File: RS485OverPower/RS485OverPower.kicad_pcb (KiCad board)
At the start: 2 copper layers, 50 x 45 mm, 27 parts, among them J101 OSTTC022162, J102 OSTTC022162, U101 RT6200, U102 LT1785xS8

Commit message: First layout done
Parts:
- removed R101: R_Small, Resistor_SMD:R_0603_1608Metric
- added C111: 1u/10V, Capacitor_SMD:C_0603_1608Metric, F.Cu at (106.6, 55.0)
- added C112: 1u/10V, Capacitor_SMD:C_0603_1608Metric, F.Cu at (87.7, 78.4)
- C101: footprint Capacitor_SMD:C_0603_1608Metric -> Capacitor_SMD:C_0805_2012Metric
- L101, L102, L103: value 47u -> 33UH; footprint digikey-footprints:1210 -> PCBDecals:MWSA0603
- moved C109 69.3 mm to (74.9, 88.0)
- moved C107 65.9 mm to (75.1, 90.1)
- moved R106 49.6 mm to (83.9, 80.1), turned to 180 degrees
- moved C101 44.3 mm to (101.8, 83.3), turned to 180 degrees
- moved R108 37.4 mm to (100.4, 75.4), turned to 180 degrees
- moved R107 37.1 mm to (104.7, 75.4), turned to 180 degrees
- moved C108 35.8 mm to (109.5, 74.3), turned to 90 degrees
- moved C110 28.9 mm to (111.3, 74.4), turned to 90 degrees
- moved L101 12.5 mm to (110.3, 79.9), turned to 0 degrees
- moved C106 12.0 mm to (107.3, 74.3), turned to 90 degrees
- moved R102 10.8 mm to (101.7, 81.0)
- moved L103 10.5 mm to (90.9, 83.6)
- moved R103 9.71 mm to (99.7, 78.5)
- moved C102 9.71 mm to (98.1, 78.5)
- moved U101 9.71 mm to (102.5, 78.2)
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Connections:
- net Net-(R107-Pad2) renamed /FB
- A101 pad 18: VCC -> Net-(A101-Pad18)
- A101 pad 3: Net-(A101-Pad28) -> Net-(A101-Pad3)
- C103 pad 2: Net-(C103-Pad2) -> /SW
- D101 pad 1: Net-(C103-Pad2) -> /SW
- L101 pad 1: VCC -> /SW
- L101 pad 2: Net-(C103-Pad2) -> VCC
- U101 pad 6: Net-(C103-Pad2) -> /SW
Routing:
- net VCC: track 0.00 -> 56.2 mm
- net +24V: track 23.9 -> 52.9 mm, vias 1 -> 2
- net Net-(A101-Pad1): track 4.16 -> 10.5 mm
- net /FB: track 0.00 -> 6.19 mm
- net Net-(A101-Pad2): track 4.02 -> 9.72 mm
- net Net-(A101-Pad6): track 20.9 -> 15.5 mm
- net Net-(C102-Pad1): track 0.00 -> 5.26 mm
- net GND: track 0.00 -> 4.38 mm, vias 0 -> 19
- net Net-(A101-Pad5): track 15.1 -> 12.6 mm
- net Net-(A101-Pad18): track 0.00 -> 2.34 mm
- net Net-(C103-Pad1): track 0.00 -> 1.88 mm
- net Net-(C104-Pad2): track 2.93 -> 4.57 mm
- net Net-(C105-Pad1): track 3.15 -> 4.57 mm
- net Net-(C105-Pad2): track 10.0 -> 11.1 mm
- net Net-(C104-Pad1): track 10.4 -> 11.0 mm
- added copper zone on B.Cu, net +24V
- added copper zone on F.Cu, net /SW
- added copper zone on B.Cu, net GND
- added copper zone on F.Cu, net GND
- added copper zone on F.Cu, net VCC
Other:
- rule pad_to_mask_clearance: 0 -> 0.1

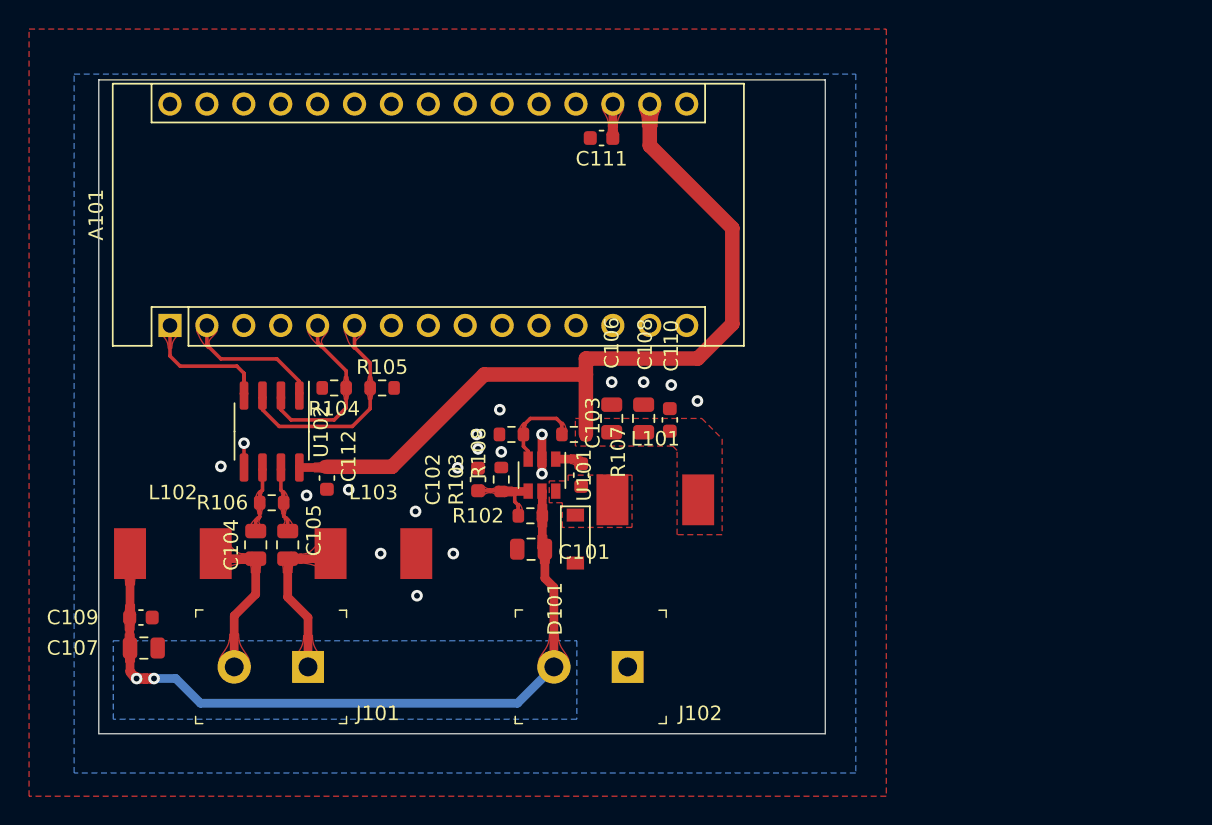
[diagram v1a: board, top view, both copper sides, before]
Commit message: Added connector for I/O
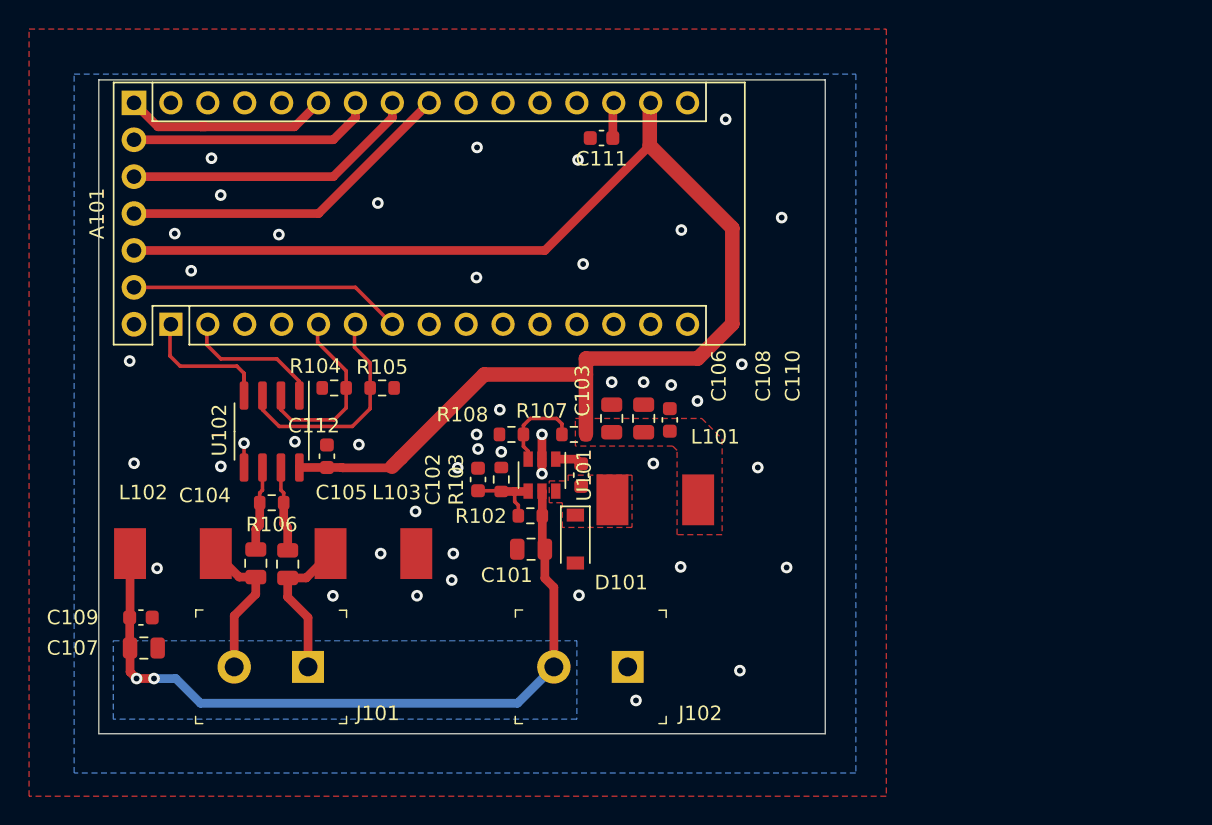
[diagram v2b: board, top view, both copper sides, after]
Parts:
- added J103: Conn_01x07, Connector_PinHeader_2.54mm:PinHeader_1x07_P2.54mm_Vertical, B.Cu at (74.4, 52.6)
- moved C112 1.50 mm to (87.7, 76.9), turned to 90 degrees
- moved C105 1.33 mm to (85.0, 84.3)
- moved C104 1.27 mm to (82.8, 84.3)
- moved A101 0.10 mm to (77.0, 67.8)
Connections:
- A101 pad 23: Net-(A101-Pad23) -> A4
- A101 pad 24: Net-(A101-Pad24) -> A5
- A101 pad 25: Net-(A101-Pad25) -> A6
- A101 pad 26: Net-(A101-Pad26) -> A7
- A101 pad 7: Net-(A101-Pad7) -> D4
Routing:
- net VCC: track 56.2 -> 95.5 mm
- net A4: track 0.00 -> 23.5 mm
- net A7: track 0.00 -> 20.5 mm
- net A5: track 0.00 -> 20.5 mm
- net D4: track 0.00 -> 18.8 mm
- net A6: track 0.00 -> 16.9 mm
- net Net-(C105-Pad1): track 4.57 -> 5.90 mm
- net Net-(C104-Pad2): track 4.57 -> 5.83 mm
- net GND: vias 19 -> 45

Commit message: Layout improvements
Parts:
- added H101: MountingHole, MountingHole:MountingHole_3.2mm_M3, B.Cu at (95.1, 58.5)
- added H102: MountingHole, MountingHole:MountingHole_3.2mm_M3, B.Cu at (95.1, 90.6)
- added H103: MountingHole, MountingHole:MountingHole_3.2mm_M3, B.Cu at (117.4, 58.5)
- added H104: MountingHole, MountingHole:MountingHole_3.2mm_M3, B.Cu at (116.1, 90.6)
- moved L102 1.00 mm to (77.1, 82.6)
- moved L103 1.00 mm to (90.9, 82.6)
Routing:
- net +24V: track 52.9 -> 12.5 mm, vias 2 -> 6
- net A4: track 23.5 -> 12.7 mm
- net VCC: track 95.5 -> 92.7 mm
- net A7: track 20.5 -> 18.2 mm
- added copper zone on F.Cu, net +24V
